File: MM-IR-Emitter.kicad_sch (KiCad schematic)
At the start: 7 parts, among them U6 MOSFET

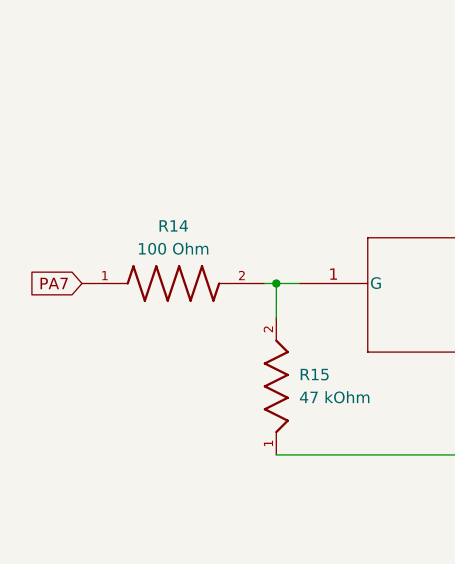
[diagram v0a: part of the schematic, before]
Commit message: added power switch
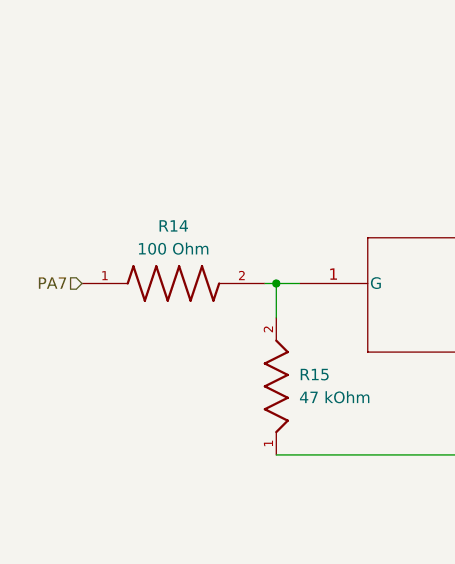
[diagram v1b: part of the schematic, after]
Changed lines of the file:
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@@
 		)
 	)
-	(global_label "PA7"
+	(hierarchical_label "PA7"
 		(shape input)
 		(at 82.55 102.87 180)
-		(fields_autoplaced yes)
 		(effects
 			(font
@@
 			(justify right)
 		)
-		(property "Intersheetrefs" "${INTERSHEET_REFS}"
-			(at 75.9967 102.87 0)
-			(effects
-				(font
-					(size 1.27 1.27)
-				)
-				(justify right)
-				(hide yes)
-			)
-		)
 	)

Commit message: fixedled orignetation and linked to ground + duplicated IR emitter/receiver pairs
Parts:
- C32: footprint 0.1µFCapacitor_footprints:CAP_0402_N_WAL-L -> Ceramic_Capacitor_0.1uF_CL21B104KBCNNNC:CAPC2012X95N
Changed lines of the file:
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@@
 			)
 		)
-		(property "Footprint" "0.1µFCapacitor_footprints:CAP_0402_N_WAL-L"
+		(property "Footprint" "Ceramic_Capacitor_0.1uF_CL21B104KBCNNNC:CAPC2012X95N"
 			(at 167.64 93.98 0)
 			(effects

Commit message: Add files via upload
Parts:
- removed C32: 0.1 µF, Ceramic_Capacitor_0.1uF_CL21B104KBCNNNC:CAPC2012X95N, symbol 0.1µFCapacitor_2025-12-15_19-47-12:0402B104K160CT
- added C8: 0.1 µF, CL05A104KA5NNNC:CAPC1005X55N, symbol 0.1µFCapacitor_CL05A104KA5NNNC:CL05A104KA5NNNC
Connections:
- net 3V3: now also C8.2
- net GND: now also C8.1
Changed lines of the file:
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@@
+	)
+	(symbol
+		(lib_id "0.1µFCapacitor_CL05A104KA5NNNC:CL05A104KA5NNNC")
+		(at 167.64 91.44 90)
+		(unit 1)
+		(exclude_from_sim no)
+		(in_bom yes)
+		(on_board yes)
+		(dnp no)
+		(fields_autoplaced yes)
+		(property "Reference" "C8"
+			(at 171.45 88.8999 90)
+			(effects
+				(font
+					(size 1.27 1.27)
+				)
+				(justify right)
+			)
+		)
+		(property "Value" "0.1 µF"
+			(at 171.45 91.4399 90)
+			(effects
+				(font
+					(size 1.27 1.27)
+				)
+				(justify right)
+			)
+		)
+		(property "Footprint" "CL05A104KA5NNNC:CAPC1005X55N"
+			(at 167.64 91.44 0)
+			(effects
+				(font
+					(size 1.27 1.27)
+				)
+				(justify bottom)
+				(hide yes)
+			)
+		)
+		(property "Datasheet" ""
+			(at 167.64 91.44 0)
+			(effects
+				(font
+					(size 1.27 1.27)
+				)
+				(hide yes)
+			)
+		)
+		(property "Description" ""
+			(at 167.64 91.44 0)
+			(effects
+				(font
+					(size 1.27 1.27)
+				)
+				(hide yes)
+			)
+		)
+		(property "E_max" "0.55"
+			(at 167.64 91.44 0)
+			(effects
+				(font
+					(size 1.27 1.27)
+				)
+				(justify bottom)
+				(hide yes)
+			)
+		)
+		(property "L_max" "0.35"
+			(at 167.64 91.44 0)
+			(effects
+				(font
+					(size 1.27 1.27)
+				)
+				(justify bottom)
+				(hide yes)
+			)
+		)
+		(property "A_max" "0.55"
+			(at 167.64 91.44 0)
+			(effects
+				(font
+					(size 1.27 1.27)
+				)
+				(justify bottom)
+				(hide yes)
+			)
+		)
+		(property "L1_nom" "0.25"
+			(at 167.64 91.44 0)
+			(effects
+				(font
+					(size 1.27 1.27)
+				)
+				(justify bottom)
+				(hide yes)
+			)
+		)
+		(property "D_max" "1.05"
+			(at 167.64 91.44 0)
+			(effects
+				(font
+					(size 1.27 1.27)
+				)
+				(justify bottom)
+				(hide yes)
+			)
+		)
+		(property "A_nom" "0.55"
+			(at 167.64 91.44 0)
+			(effects
+				(font
+					(size 1.27 1.27)
+				)
+				(justify bottom)
+				(hide yes)
+			)
+		)
+		(property "L1_max" "0.35"
+			(at 167.64 91.44 0)
+			(effects
+				(font
+					(size 1.27 1.27)
+				)
+				(justify bottom)
+				(hide yes)
+			)
+		)
+		(property "L1_min" "0.15"
+			(at 167.64 91.44 0)
+			(effects
+				(font
+					(size 1.27 1.27)
+				)
+				(justify bottom)
+				(hide yes)
+			)
+		)
+		(property "A_min" "0.55"
+			(at 167.64 91.44 0)
+			(effects
+				(font
+					(size 1.27 1.27)
+				)
+				(justify bottom)
+				(hide yes)
+			)
+		)
+		(property "E_min" "0.45"
+			(at 167.64 91.44 0)
+			(effects
+				(font
+					(size 1.27 1.27)
+				)
+				(justify bottom)
+				(hide yes)
+			)
+		)
+		(property "D_min" "0.95"
+			(at 167.64 91.44 0)
+			(effects
+				(font
+					(size 1.27 1.27)
+				)
+				(justify bottom)
+				(hide yes)
+			)
+		)
+		(property "D_nom" "1.0"
+			(at 167.64 91.44 0)
+			(effects
+				(font
+					(size 1.27 1.27)
+				)
+				(justify bottom)
+				(hide yes)
+			)
+		)
+		(property "E_nom" "0.5"
+			(at 167.64 91.44 0)
+			(effects
+				(font
+					(size 1.27 1.27)
+				)
+				(justify bottom)
+				(hide yes)
+			)
+		)
+		(property "STANDARD" "IPC 7351B"
+			(at 167.64 91.44 0)
+			(effects
+				(font
+					(size 1.27 1.27)
+				)
+				(justify bottom)
+				(hide yes)
+			)
+		)
+		(property "L_min" "0.15"
+			(at 167.64 91.44 0)
+			(effects
+				(font
+					(size 1.27 1.27)
+				)
+				(justify bottom)
+				(hide yes)
+			)
+		)
+		(property "L_nom" "0.25"
+			(at 167.64 91.44 0)
+			(effects
+				(font
+					(size 1.27 1.27)
+				)
+				(justify bottom)
+				(hide yes)
+			)
+		)
+		(property "MANUFACTURER" "Samsung Electro-Mechanics"
+			(at 167.64 91.44 0)
+			(effects
+				(font
+					(size 1.27 1.27)
+				)
+				(justify bottom)
+				(hide yes)
+			)
+		)
+		(pin "2"
+		)
+		(pin "1"
+		)
+		(instances
+			(project "IREmitter"
+				(path "/d311851a-8b0b-4acf-b2e7-1b968b2adbe7/b0ddafb5-a55e-4fac-9b6d-00a4e7161424"
+					(reference "C8")
+					(unit 1)
+				)
+			)
+		)
 	)
 	(symbol
@@
 					(unit 1)
 				)
-			)
-		)
-	)
-	(symbol
-		(lib_id "0.1µFCapacitor_2025-12-15_19-47-12:0402B104K160CT")
-		(at 167.64 93.98 90)
-		(unit 1)
-		(exclude_from_sim no)
-		(in_bom yes)
-		(on_board yes)
-		(dnp no)
-		(property "Reference" "C32"
-			(at 171.45 92.456 90)
-			(effects
-				(font
-					(size 1.524 1.524)
-				)
-				(justify left)
-			)
-		)
-		(property "Value" "0.1 µF"
-			(at 176.022 95.25 90)
-			(effects
-				(font
-					(size 1.524 1.524)
-				)
-				(justify left)
-			)
-		)
-		(property "Footprint" "Ceramic_Capacitor_0.1uF_CL21B104KBCNNNC:CAPC2012X95N"
-			(at 167.64 93.98 0)
-			(effects
-				(font
-					(size 1.27 1.27)
-					(italic yes)
-				)
-				(hide yes)
-			)
-		)
-		(property "Datasheet" "0402B104K160CT"
-			(at 167.64 93.98 0)
-			(effects
-				(font
-					(size 1.27 1.27)
-					(italic yes)
-				)
-				(hide yes)
-			)
-		)
-		(property "Description" ""
-			(at 167.64 93.98 0)
-			(effects
-				(font
-					(size 1.27 1.27)
-				)
-				(hide yes)
-			)
-		)
-		(pin "2"
-		)
-		(pin "1"
-		)
-		(instances
-			(project "IREmitter"
-				(path "/d311851a-8b0b-4acf-b2e7-1b968b2adbe7/b0ddafb5-a55e-4fac-9b6d-00a4e7161424"
-					(reference "C32")
-					(unit 1)
-				)

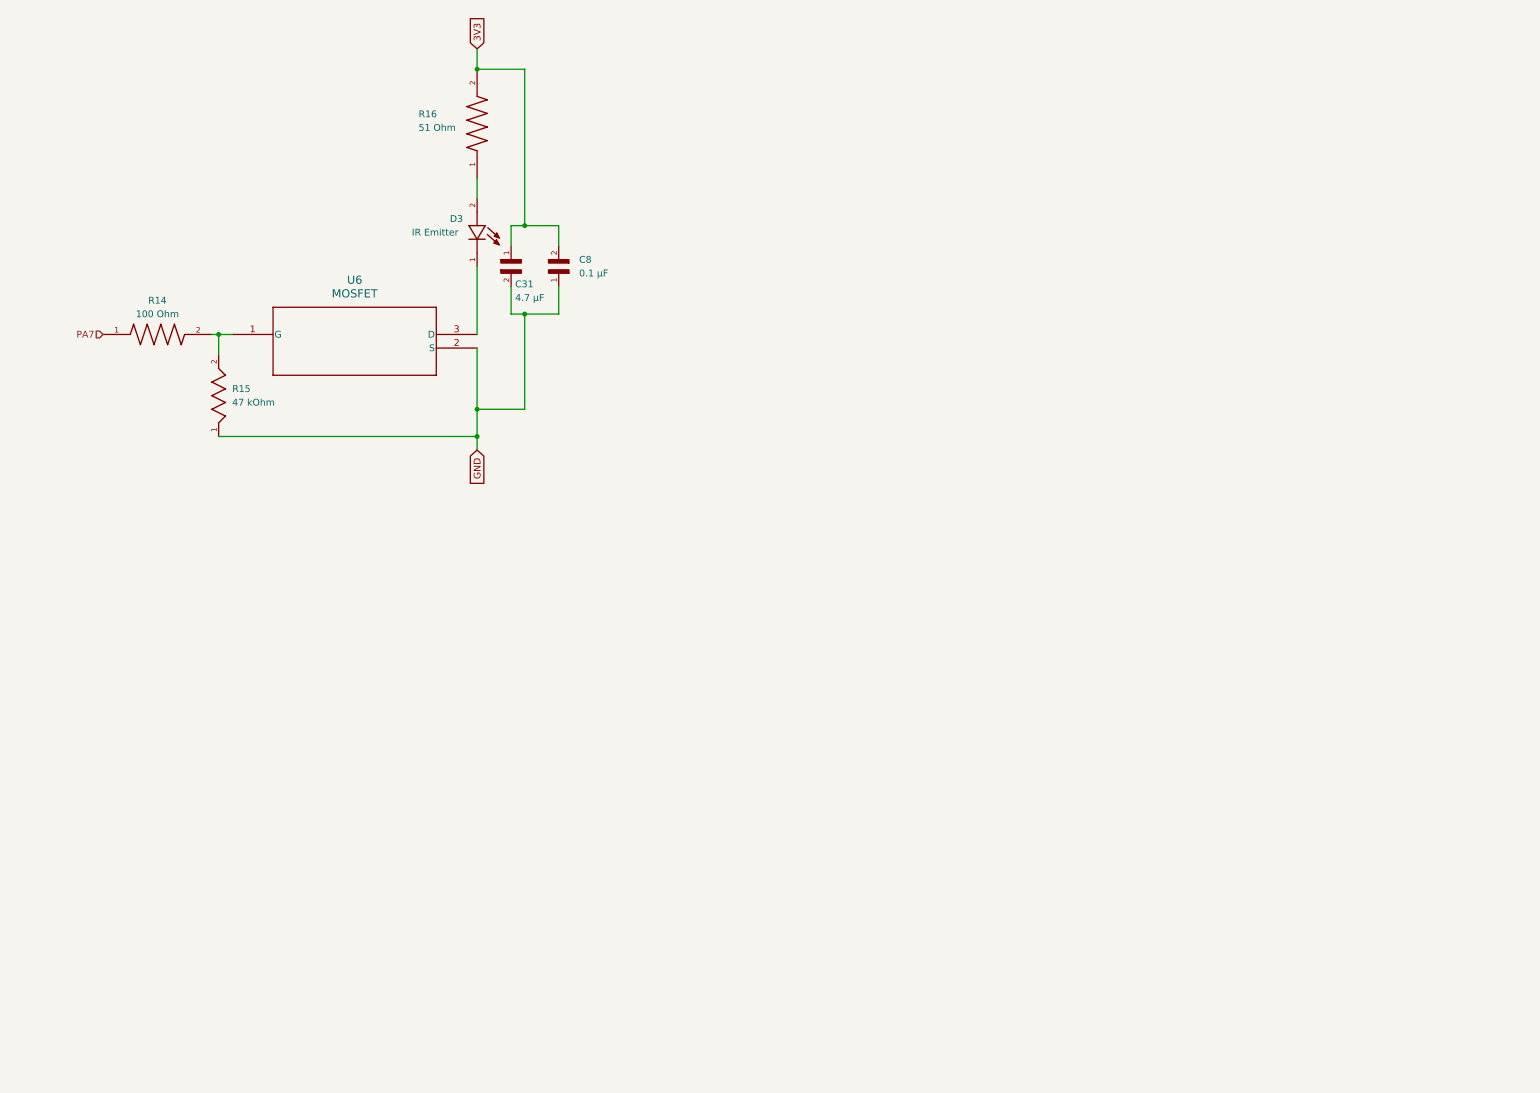
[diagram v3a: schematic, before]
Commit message: redid the 4 emitters receivers, fixed orientation of LEDS and going to continue adding footprints and replace the 60ohm resistors with 300ohm ones
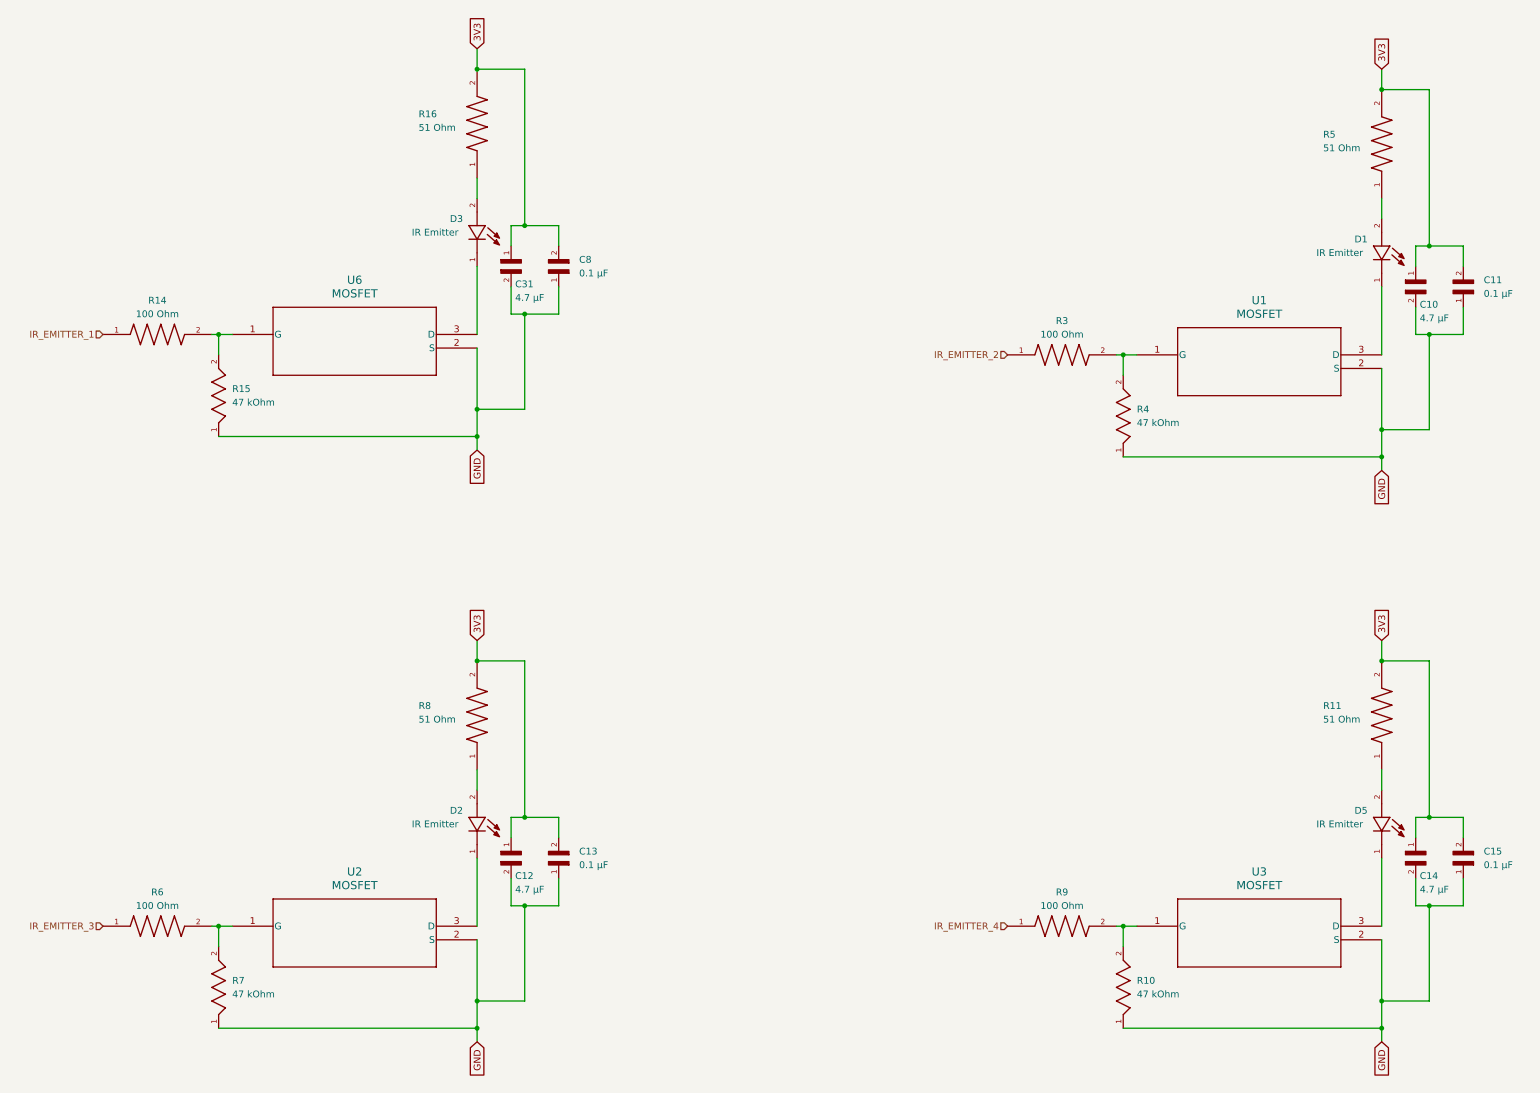
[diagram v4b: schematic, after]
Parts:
- added C10, C12, C14: 4.7 µF, Ceramic_Capacitor_4.7uF_CL21A475KAQNNNE:CAPC2012X140N, symbol 4.7µFCapacitor_CL10A475KP8NNNC:CL10A475KP8NNNC
- added C11, C13, C15: 0.1 µF, Ceramic_Capacitor_0.1uF_CL21B104KBCNNNC:CAPC2012X95N, symbol 0.1µFCapacitor_CL05A104KA5NNNC:CL05A104KA5NNNC
- added D1, D2, D5: IR Emitter, APT1608F3C:LED_APT1608F3C, symbol IRSensor_APT1608F3C:APT1608F3C
- added R10, R4, R7: 47 kOhm, RC0603FR_0747KL:RESC1608X55, symbol 47kOhmResistor_RC0603FR-0747KL:RC0603FR-0747KL
- added R11, R5, R8: 51 Ohm, RC0805FR_0751RL:RESC2012X60N, symbol 51OhmResistor_RC0805FR-0751RL:RC0805FR-0751RL
- added R3, R6, R9: 100 Ohm, CRCW0603100RFKEA:RESC1508X50N, symbol 100OhmResistor_CRCW0603100RFKEA:CRCW0603100RFKEA
- added U1, U2, U3: MOSFET, MOSFET_footprints:SOT-23_1_DIO, symbol MOSFET_2026-01-14_23-16-18:2N7002-7-F
- C31: footprint CL10A475KP8NNNC:CAPC1608X90N -> Ceramic_Capacitor_4.7uF_CL21A475KAQNNNE:CAPC2012X140N
- C8: footprint CL05A104KA5NNNC:CAPC1005X55N -> Ceramic_Capacitor_0.1uF_CL21B104KBCNNNC:CAPC2012X95N
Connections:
- net 3V3: now also C10.1, C11.2, C12.1, C13.2, C14.1, C15.2, R11.2, R5.2, R8.2
- net GND: now also C10.2, C11.1, C12.2, C13.1, C14.2, C15.1, R10.1, R4.1, R7.1, U1.2 (S), U2.2 (S), U3.2 (S)
- net PA7 renamed IR_EMITTER_1
- new net: R3.2, R4.2, U1.1 (G)
- new net: D1.1, U1.3 (D)
- new net: R10.2, R9.2, U3.1 (G)
- new net: D5.2, R11.1
- new net: D1.2, R5.1
- new net: R6.2, R7.2, U2.1 (G)
- new net: D5.1, U3.3 (D)
- new net: D2.1, U2.3 (D)
- new net: D2.2, R8.1
- new net IR_EMITTER_2: R3.1
- new net IR_EMITTER_3: R6.1
- new net IR_EMITTER_4: R9.1

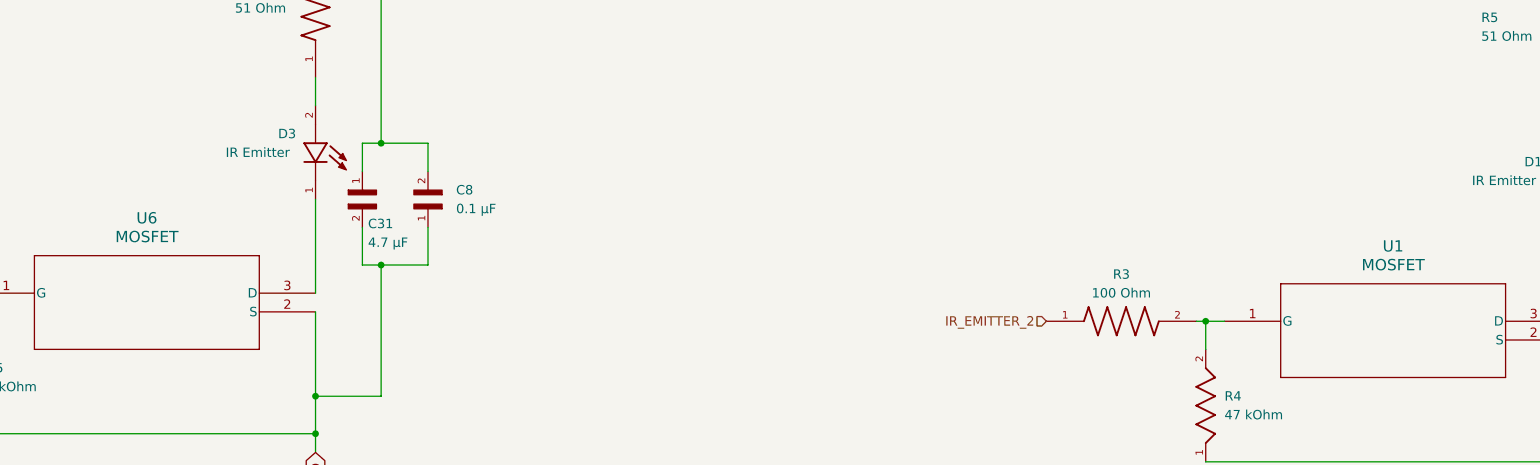
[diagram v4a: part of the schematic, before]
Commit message: finished adding rest of footprints, tried replacing mosfets with no success
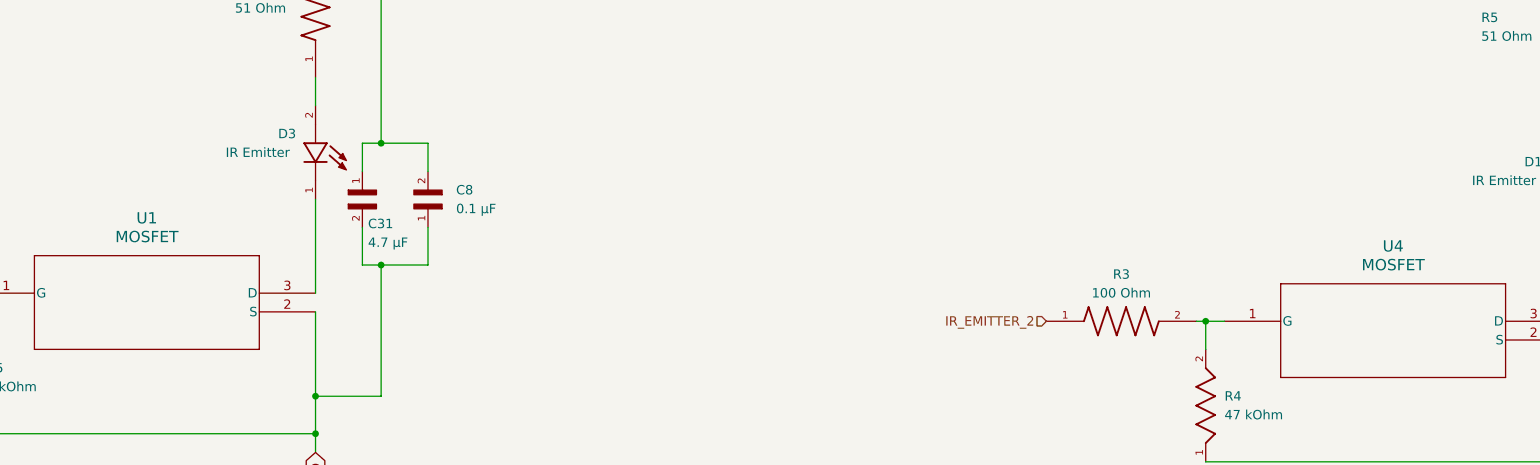
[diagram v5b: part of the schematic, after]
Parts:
- removed U1, U2, U3, U6: MOSFET, MOSFET_footprints:SOT-23_1_DIO, symbol MOSFET_2026-01-14_23-16-18:2N7002-7-F
- added U1, U2, U3, U4: MOSFET, symbol MOSFET_ul_2N7002-7-F:2N7002-7-F
- D1, D2, D3, D5: footprint APT1608F3C:LED_APT1608F3C -> IR_Emitter_APT1608F3C:LED_APT1608F3C
- R10, R15, R4, R7: footprint RC0603FR_0747KL:RESC1608X55 -> 47_kohm_RC0603FR-0747KL:RESC1608X55
- R11, R16, R5, R8: footprint RC0805FR_0751RL:RESC2012X60N -> 51_ohm_RC0805FR-0751RL:RESC2012X60N
- R14, R3, R6, R9: footprint CRCW0603100RFKEA:RESC1508X50N -> 100_ohm_CRCW0603100RFKEA:RESC1508X50N
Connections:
- net GND: now also U1.2 (S), U2.2 (S), U3.2 (S), U4.2 (S)
- net at R3.2, R4.2: now also U4.1 (G)
- net at D1.1: now also U4.3 (D)
- net at R14.2, R15.2: now also U1.1 (G)
- net at D3.1: now also U1.3 (D)
- net at R10.2, R9.2: now also U3.1 (G)
- net at R6.2, R7.2: now also U2.1 (G)
- net at D5.1: now also U3.3 (D)
- net at D2.1: now also U2.3 (D)

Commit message: LED changes, mosfet footprint fixed
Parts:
- U1, U2, U3, U4: footprint (none) -> MOSFET_ul_2N7002-7-F:SOT-23_1_DIO
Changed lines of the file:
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@@
 			)
 		)
-		(property "Footprint" ""
+		(property "Footprint" "MOSFET_ul_2N7002-7-F:SOT-23_1_DIO"
 			(at 106.68 213.36 0)
 			(effects
@@
 			)
 		)
-		(property "Footprint" ""
+		(property "Footprint" "MOSFET_ul_2N7002-7-F:SOT-23_1_DIO"
 			(at 106.68 102.87 0)
 			(effects
@@
 			)
 		)
-		(property "Footprint" ""
+		(property "Footprint" "MOSFET_ul_2N7002-7-F:SOT-23_1_DIO"
 			(at 275.59 213.36 0)
 			(effects
@@
 			)
 		)
-		(property "Footprint" ""
+		(property "Footprint" "MOSFET_ul_2N7002-7-F:SOT-23_1_DIO"
 			(at 275.59 106.68 0)
 			(effects

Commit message: PCB tentative finished
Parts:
- removed D1, D2, D3, D5: IR Emitter, IR_Emitter_APT1608F3C:LED_APT1608F3C, symbol IRSensor_APT1608F3C:APT1608F3C
- added D1, D2, D3, D4: IR Emitter, IR_Emitter_TSAL6400:LEDRD254W55D595H900, symbol IR_Emitter_TSAL6400:TSAL6400
- renumbered U4 to U2, U2 to U3, U3 to U4
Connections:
- net at U3.3 (D): now also D3.C
- net at R11.1: now also D4.A
- net at U2.3 (D): now also D2.C
- net at R5.1: now also D2.A
- net at U1.3 (D): now also D1.C
- net at R16.1: now also D1.A
- net at R8.1: now also D3.A
- net at U4.3 (D): now also D4.C
